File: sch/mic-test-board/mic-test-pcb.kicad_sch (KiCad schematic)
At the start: 46 parts, among them J1 Conn_02x05_Odd_Even, J2 Conn_01x02, U1 NCP163ASN180T1G, U2 SN74LVC2T45DCUR

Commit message: feat: schematic WIP
 - Analog front end 99% selected and wired up
 - uController/dev board interface 1% done
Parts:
- removed C1 (x2): 0.1uF, Capacitor_SMD:C_0603_1608Metric, symbol Device:C_Small
- removed C1: 1uF, Capacitor_SMD:C_0603_1608Metric, symbol Device:C_Small
- removed C1 (x2): 22pF, Capacitor_SMD:C_0603_1608Metric, symbol Device:C_Small
- removed D1: LED_Small_Filled, LED_SMD:LED_0805_2012Metric, symbol Device:LED_Small_Filled
- removed J2: Conn_01x02, Connector_PinHeader_2.54mm:PinHeader_1x02_P2.54mm_Vertical, symbol Connector_Generic:Conn_01x02
- removed JP1, JP10, JP11, JP12, JP13, JP14, JP15, JP2, JP3, JP4, JP5, JP6, JP7, JP8, JP9: SolderJumper_2_Open, Jumper:SolderJumper-2_P1.3mm_Open_TrianglePad1.0x1.5mm, symbol Jumper:SolderJumper_2_Open
- removed JP16, JP17: SolderJumper_3_Open, Jumper:SolderJumper-3_P2.0mm_Open_TrianglePad1.0x1.5mm_NumberLabels, symbol Jumper:SolderJumper_3_Open
- removed R1, R5, R51, R53: 68.1R, Resistor_SMD:R_0603_1608Metric, symbol Device:R_Small
- removed R4: 0R, Resistor_SMD:R_0603_1608Metric, symbol Device:R_Small
- removed R8: 180R, Resistor_SMD:R_0603_1608Metric, symbol Device:R_Small
- removed TP1, TP5, TP6: TestPoint, TestPoint:TestPoint_Pad_D1.5mm, symbol Connector:TestPoint
- removed U1: NCP163ASN180T1G, Package_TO_SOT_SMD:SOT-23-5, symbol Regulator_Linear:NCP163ASN180T1G
- removed U2: SN74LVC2T45DCUR, Package_SO:VSSOP-8_2.4x2.1mm_P0.5mm, symbol Logic_LevelTranslator:SN74LVC2T45DCUR
- renumbered C1 to C18, C1 to C20
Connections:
- no-connect marks 1 -> 6
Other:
- removed sheet Mic1
- removed sheet Mic10
- removed sheet Mic11
- removed sheet Mic12
- removed sheet Mic13
- removed sheet Mic14
- removed sheet Mic15
- removed sheet Mic16
- removed sheet Mic2
- removed sheet Mic3
- removed sheet Mic4
- removed sheet Mic5
- removed sheet Mic6
- removed sheet Mic7
- removed sheet Mic8
- removed sheet Mic9
- added sheet ADC AD7768 (ADC_AD7768.kicad_sch)
- added sheet ADC AD7769 (ADC_AD7768.kicad_sch)
- added sheet ADC Common parts (ADCCommonParts.kicad_sch)
- added sheet AnalogFrontEnd (AnalogFrontEnd.kicad_sch)
- added sheet Power (Power.kicad_sch)
- added sheet uController (uController.kicad_sch)
- note removed: "1.8V Supply"
- note removed: "IC-52000 mics draw 1mA"
- note removed: "SD Termination resistor"
- note removed: "Vf = 1.85V"

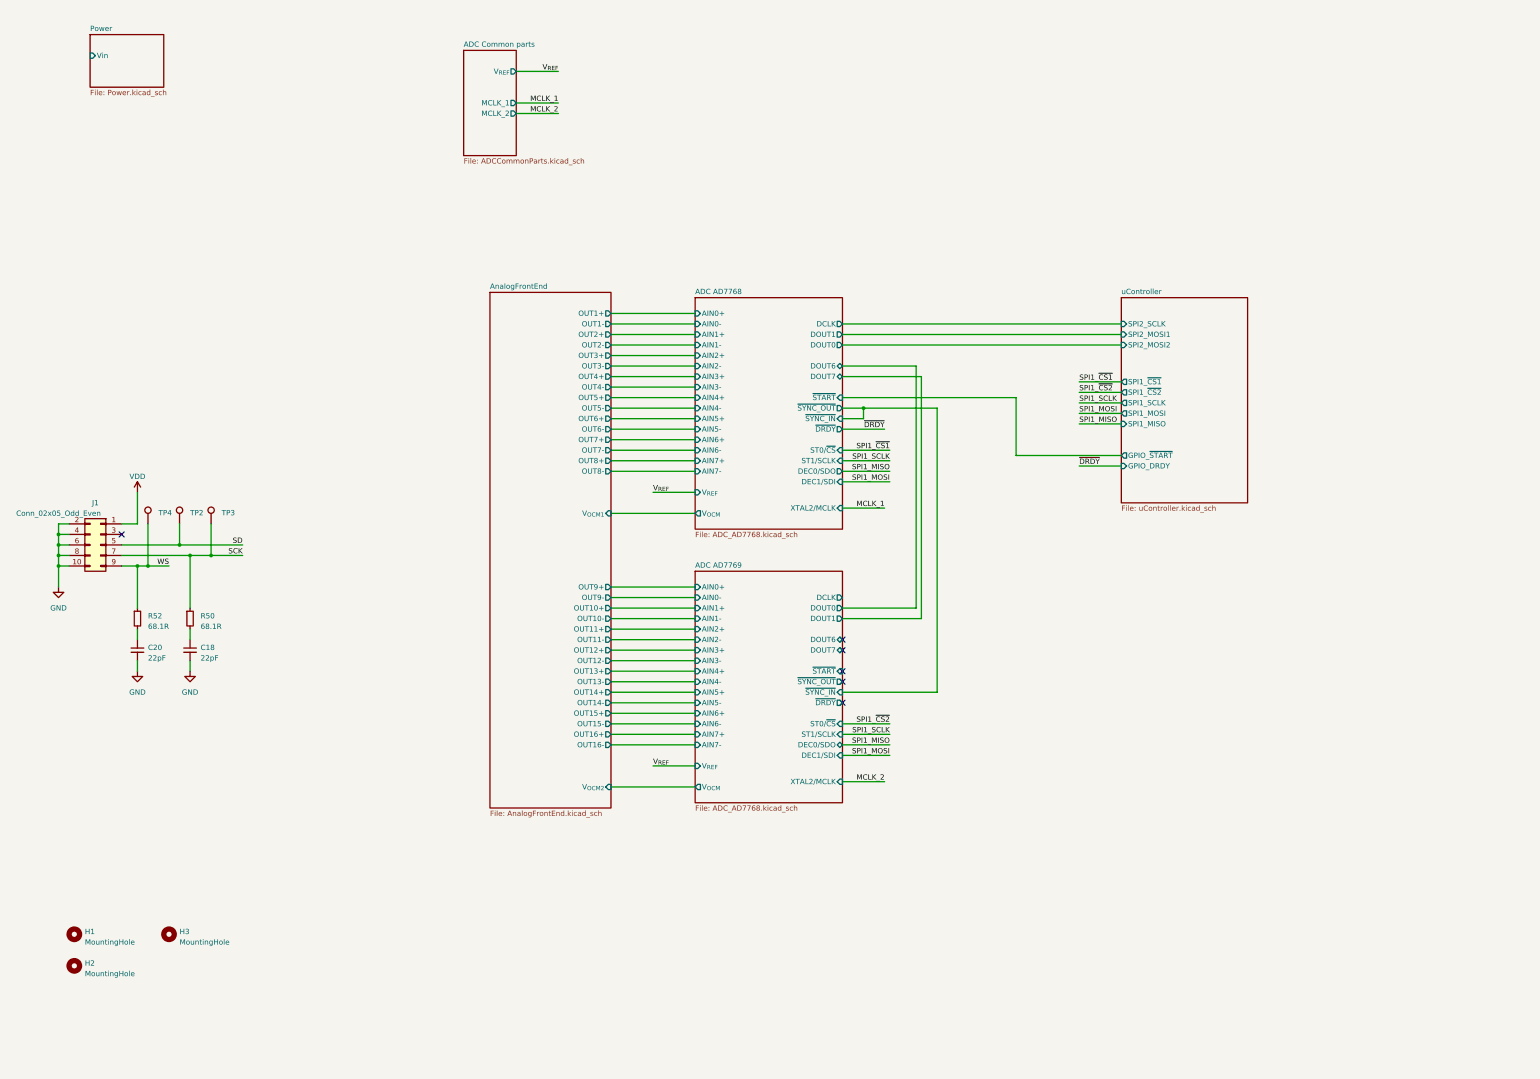
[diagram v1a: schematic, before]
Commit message: pcb: commit before large routing effort
 - schematic refactor to split preamps to each mic board
 - Mic board and main board are placed
 - no tracks laid
 - critical parts selected
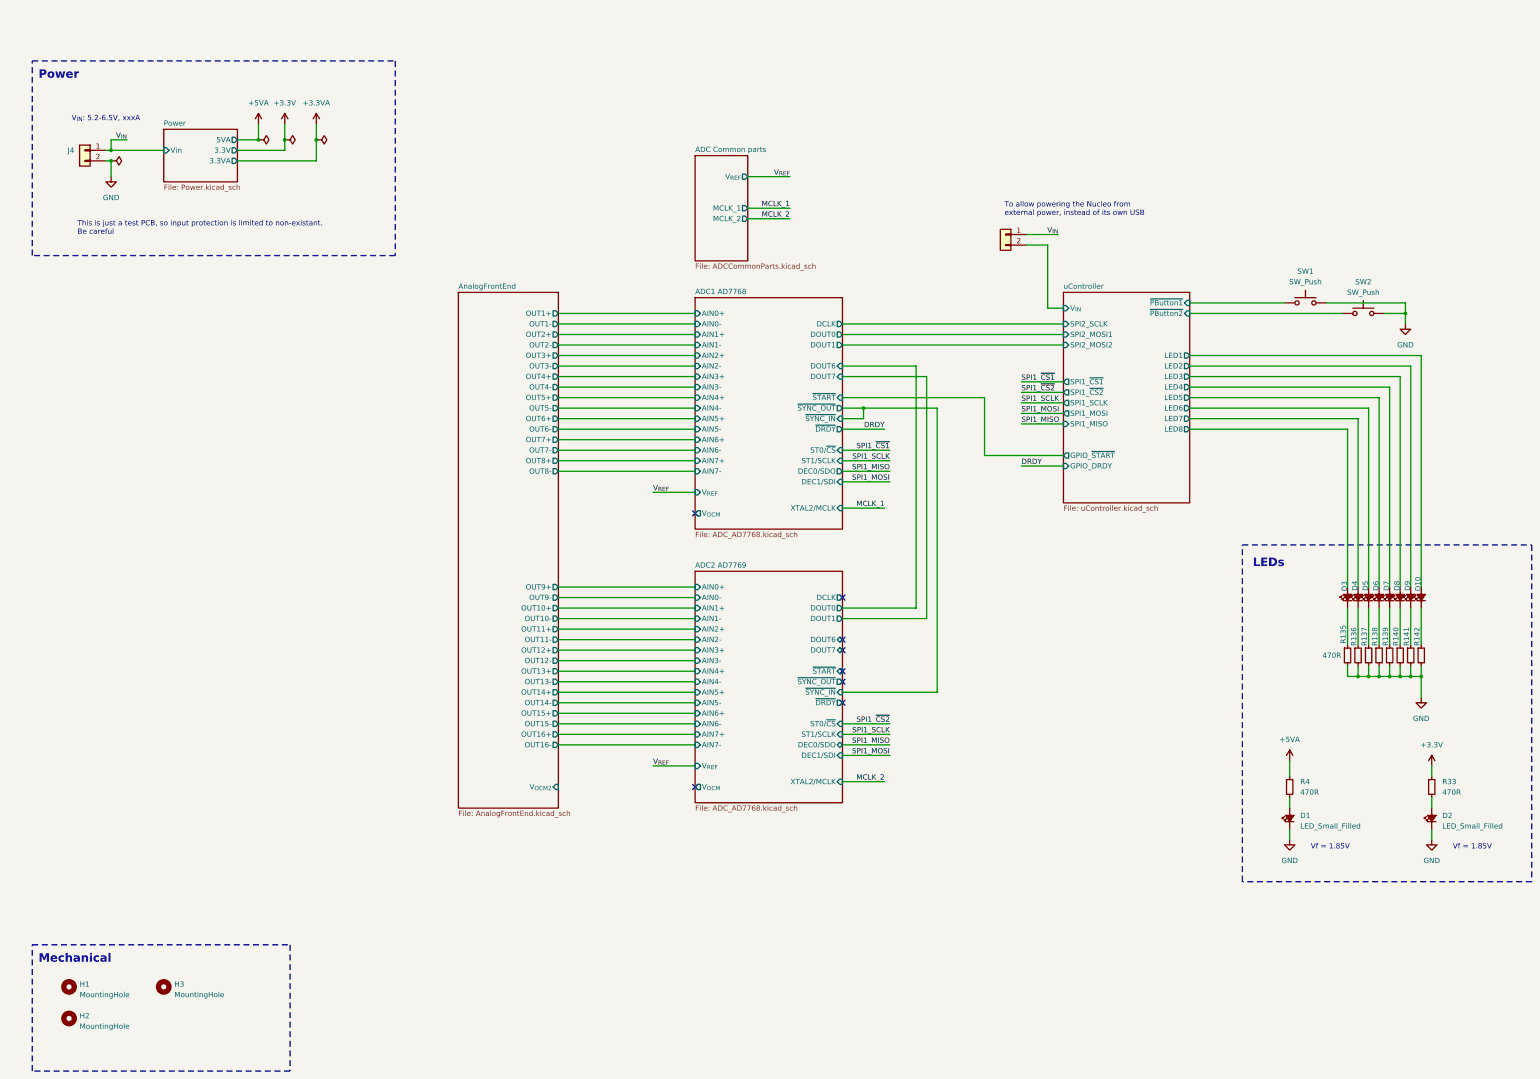
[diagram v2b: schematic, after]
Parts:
- removed C18, C20: 22pF, Capacitor_SMD:C_0603_1608Metric, symbol Device:C_Small
- removed J1: Conn_02x05_Odd_Even, Connector_PinHeader_2.54mm:PinHeader_2x05_P2.54mm_Vertical, symbol Connector_Generic:Conn_02x05_Odd_Even
- removed R50, R52: 68.1R, Resistor_SMD:R_0603_1608Metric, symbol Device:R_Small
- removed TP2, TP4: (no value), TestPoint:TestPoint_Pad_D1.5mm, symbol Connector:TestPoint
- removed TP3: TestPoint, TestPoint:TestPoint_Pad_D1.5mm, symbol Connector:TestPoint
- added D1, D10, D2, D3, D4, D5, D6, D7, D8, D9: LED_Small_Filled, LED_SMD:LED_0805_2012Metric, symbol Device:LED_Small_Filled
- added J3: Conn_01x03, Connector_PinHeader_2.54mm:PinHeader_1x02_P2.54mm_Vertical, symbol Connector_Generic:Conn_01x02
- added J4: Conn_01x03, TerminalBlock_Phoenix:TerminalBlock_Phoenix_MKDS-1,5-2_1x02_P5.00mm_Horizontal, symbol Connector_Generic:Conn_01x02
- added R135, R136, R137, R138, R139, R140, R141, R142, R33, R4: 470R, Resistor_SMD:R_0603_1608Metric, symbol Device:R_Small
- added SW1, SW2: SW_Push, Button_Switch_SMD:SW_SPST_CK_RS282G05A3, symbol Switch:SW_Push
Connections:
- net GND: now also D1.1 (K), D2.1 (K), J4.2 (Pin_2), R135.2, R136.2, R137.2, R138.2, R139.2, R140.2, R141.2, R142.2, SW1.2, SW2.2
- new net: D3.1 (K), R135.1
- new net: D5.1 (K), R137.1
- new net: D4.1 (K), R136.1
- new net: D8.1 (K), R140.1
- new net: D6.1 (K), R138.1
- new net: D10.1 (K), R142.1
- new net: D1.2 (A), R4.2
- new net: D2.2 (A), R33.2
- new net: D7.1 (K), R139.1
- new net: D9.1 (K), R141.1
- new net +3.3V: R33.1
- new net +5VA: R4.1
- new net V_{IN}: J3.1 (Pin_1), J4.1 (Pin_1)
- new net uController/LED1: D10.2 (A)
- new net uController/LED2: D9.2 (A)
- new net uController/LED3: D8.2 (A)
- new net uController/LED4: D7.2 (A)
- new net uController/LED5: D6.2 (A)
- new net uController/LED6: D5.2 (A)
- new net uController/LED7: D4.2 (A)
- new net uController/LED8: D3.2 (A)
- new net uController/V_{IN}: J3.2 (Pin_2)
- new net uController/~{PButton1}: SW1.1
- new net uController/~{PButton2}: SW2.1
- no-connect marks 6 -> 8
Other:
- sheet ADC AD7768 renamed ADC1 AD7768
- sheet ADC AD7769 renamed ADC2 AD7769
- sheet AnalogFrontEnd ports: added none; removed V_{OCM1}
- sheet Power ports: added 3.3V, 3.3VA, 5VA; removed none
- sheet uController ports: added LED1, LED2, LED3, LED4, LED5, LED6, LED7, LED8, V_{IN}, ~{PButton1}, ~{PButton2}; removed none
- note added: "LEDs"
- note added: "Mechanical"
- note added: "Power"
- note added: "This is just a test PCB, so input protection is limited to non-existant. Be careful"
- note added: "To allow powering the Nucleo from external power, instead of its own USB"
- note added: "V_{IN}: 5.2-6.5V, xxxA"
- note added: "Vf = 1.85V"
- company: (none) -> Josh Berry
- title: (none) -> Sound Compass POC
- moved on the sheet: H1, H2, H3

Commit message: pcb: finished routing mic board and ADC board.
 - BOM complete
 - uController pinout configured with CubeMX and re-checked
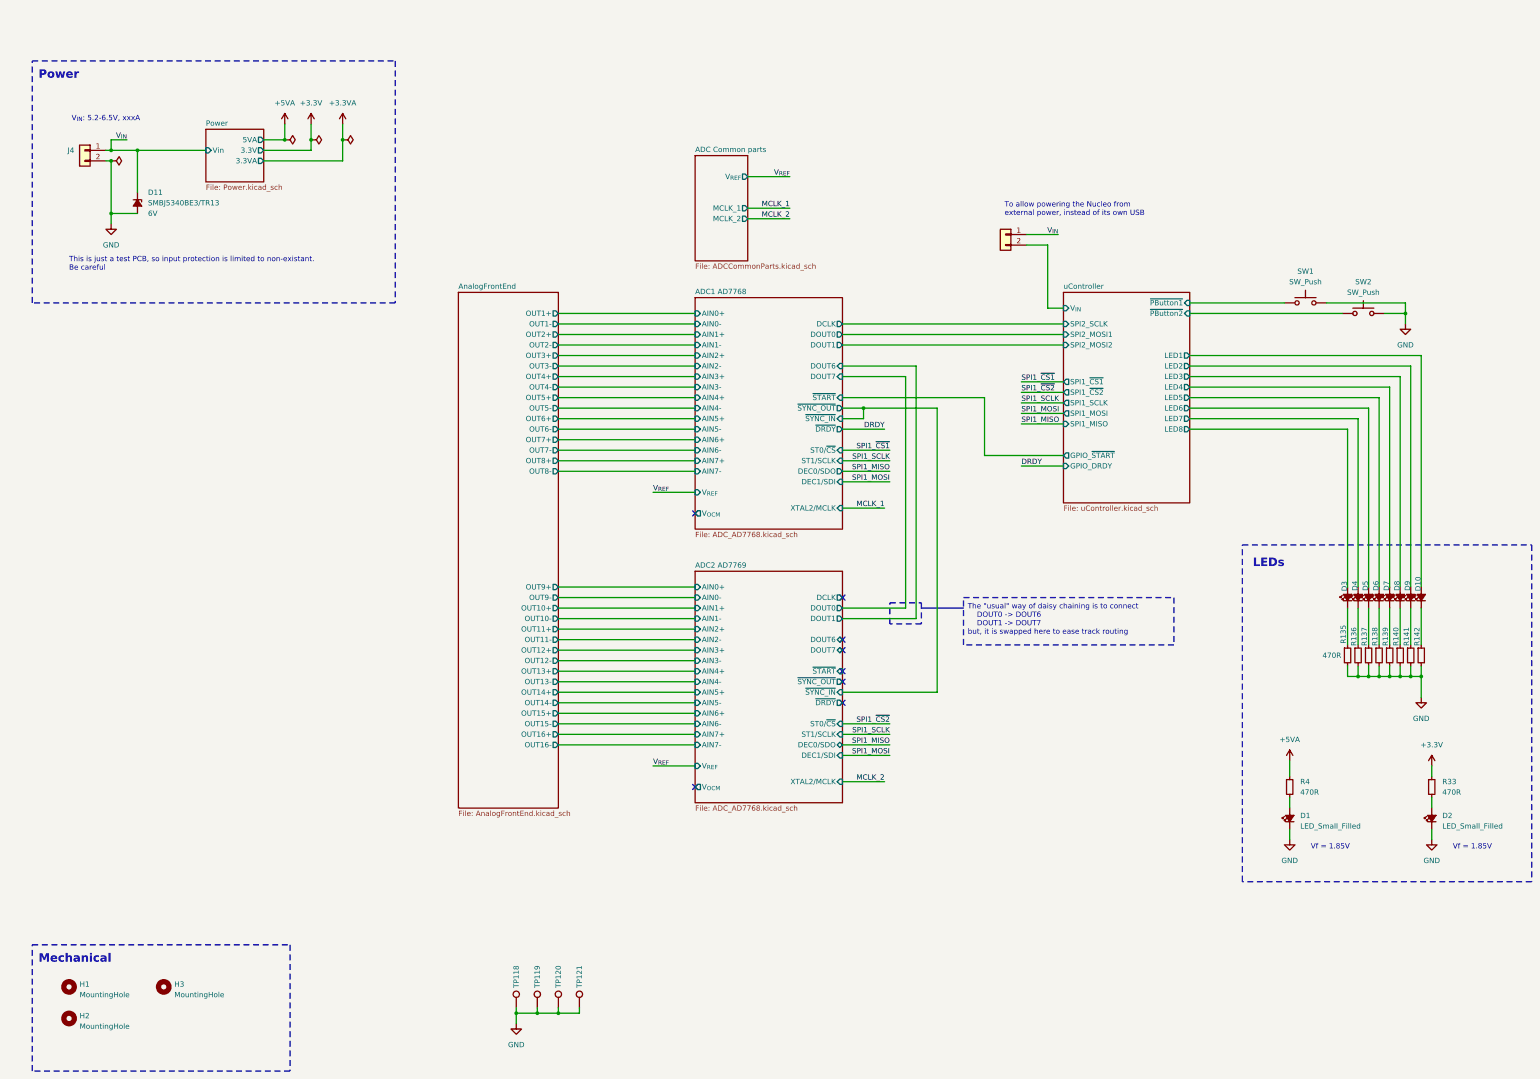
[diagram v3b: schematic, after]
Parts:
- added D11: SMBJ5340BE3/TR13, Diode_SMD:D_SMB, symbol Device:D_Zener_Small_Filled
- added TP118: 5019, TestPoint:TestPoint_Keystone_5019_Minature, symbol Connector:TestPoint
- added TP119, TP120, TP121: Hole_1.5mm, TestPoint:TestPoint_Keystone_5019_Minature, symbol Connector:TestPoint
- J4: Manufacturer (none) -> Phoenix Contact; Part Number (none) -> 1715022; Supplier (none) -> Digi-Key; Supplier Number (none) -> 277-1258-ND
- R135, R136, R137, R138, R139, R140, R141, R142, R33, R4: Manufacturer (none) -> YAGEO; Part Number (none) -> RC0603JR-07470RL; Supplier (none) -> Digi-Key; Supplier Number (none) -> 311-470GRCT-ND
- SW1, SW2: Manufacturer (none) -> C&K; Part Number (none) -> RS-282G05A3-SM RT; Supplier (none) -> Digi-Key; Supplier Number (none) -> CKN10384CT-ND
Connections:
- net GND: now also D11.2 (A), TP118.1, TP119.1, TP120.1, TP121.1
- net V_{IN}: now also D11.1 (K)
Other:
- sheet AnalogFrontEnd ports: added none; removed V_{OCM2}
- note added: "The "usual" way of daisy chaining is to connect DOUT0 -> DOUT6 DOUT1 -> DOUT7 but, it is swapped here to ease track routing"

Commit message: pcb: ordered PCB's and BOM! RevA and v240506
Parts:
- removed H1, H2, H3: MountingHole, MountingHole:MountingHole_3.2mm_M3, symbol Mechanical:MountingHole
- J3, J4: value Conn_01x03 -> Conn_01x02
